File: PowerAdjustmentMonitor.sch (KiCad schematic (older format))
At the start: 19 parts

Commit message: Started Layout Outline.  Completed other schem videos
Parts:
- removed R? (x2): R, ~, symbol R
- removed U? (x2): LM324, symbol LM324
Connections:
- net V+_MON is gone; now on net V+_ADJ: R?.1, U?.3 (OUT)
- net V-_MON is gone; now on net V-_ADJ: R?.2, U?.3 (OUT)
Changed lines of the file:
@@
 $Descr A4 11693 8268
 encoding utf-8
-Sheet 9 9
+Sheet 6 9
 Title ""
-Date "11 feb 2014"
+Date "17 feb 2014"
 Rev ""
 Comp ""
@@
 Connection ~ 3650 1650
 Wire Wire Line
-	3450 1100 4150 1100
-Wire Wire Line
-	4650 1100 5700 1100
+	3450 1100 5700 1100
 Connection ~ 3650 1100
 Text HLabel 5700 1100 2    60   Output ~ 0
@@
 Text HLabel 6750 5450 2    60   Output ~ 0
 V-_ADJ_MON
-Text HLabel 9900 1650 2    60   Output ~ 0
-V+_CURR_MON
-Text HLabel 9800 5750 2    60   Output ~ 0
-V-_CURR_MON
 $Comp
 L R R?
@@
 Wire Wire Line
 	6400 3550 6400 3450
-$Comp
-L R R?
-U 1 1 52F83066
-P 4400 1100
-F 0 "R?" V 4480 1100 40  0000 C CNN
-F 1 "R" V 4407 1101 40  0000 C CNN
-F 2 "~" V 4330 1100 30  0000 C CNN
-F 3 "~" H 4400 1100 30  0000 C CNN
-	1    4400 1100
-	0    -1   -1   0
-$EndComp
-$Comp
-L R R?
-U 1 1 52F830FF
-P 4600 7000
-F 0 "R?" V 4680 7000 40  0000 C CNN
-F 1 "R" V 4607 7001 40  0000 C CNN
-F 2 "~" V 4530 7000 30  0000 C CNN
-F 3 "~" H 4600 7000 30  0000 C CNN
-	1    4600 7000
-	0    -1   -1   0
-$EndComp
-Wire Wire Line
-	3450 7000 4350 7000
-Wire Wire Line
-	4850 7000 5900 7000
-Wire Wire Line
-	3950 1100 3950 1550
-Wire Wire Line
-	3950 1550 8200 1550
+Wire Wire Line
+	3450 7000 5900 7000
 Connection ~ 3950 1100
-Text Label 4150 1550 0    60   ~ 0
-V+_MON
-Wire Wire Line
-	4150 7000 4150 7500
-Wire Wire Line
-	4150 7500 6900 7500
-Connection ~ 4150 7000
-Text Label 4400 7500 0    60   ~ 0
-V-_MON
-$Comp
-L LM324 U?
-U 1 1 52F836D4
-P 8700 1650
-F 0 "U?" H 8750 1850 60  0000 C CNN
-F 1 "LM324" H 8850 1450 50  0000 C CNN
-F 2 "" H 8700 1650 60  0000 C CNN
-F 3 "" H 8700 1650 60  0000 C CNN
-	1    8700 1650
-	1    0    0    -1
-$EndComp
-$Comp
-L +12V #PWR?
-U 1 1 52F836ED
-P 8600 1150
-F 0 "#PWR?" H 8600 1100 20  0001 C CNN
-F 1 "+12V" H 8600 1250 30  0000 C CNN
-F 2 "" H 8600 1150 60  0000 C CNN
-F 3 "" H 8600 1150 60  0000 C CNN
-	1    8600 1150
-	1    0    0    -1
-$EndComp
-$Comp
-L -12V #PWR?
-U 1 1 52F836F3
-P 8950 2100
-F 0 "#PWR?" H 8950 2230 20  0001 C CNN
-F 1 "-12V" H 8950 2200 30  0000 C CNN
-F 2 "" H 8950 2100 60  0000 C CNN
-F 3 "" H 8950 2100 60  0000 C CNN
-	1    8950 2100
-	1    0    0    -1
-$EndComp
-Wire Wire Line
-	8200 1750 8050 1750
-Wire Wire Line
-	8050 1750 8050 2250
-Wire Wire Line
-	8050 2250 9350 2250
-Wire Wire Line
-	9350 2250 9350 1650
-Wire Wire Line
-	9200 1650 9900 1650
-Wire Wire Line
-	8600 2050 8600 2150
-Wire Wire Line
-	8600 2150 8950 2150
-Wire Wire Line
-	8950 2150 8950 2100
-Wire Wire Line
-	8600 1250 8600 1150
-Connection ~ 9350 1650
-$Comp
-L LM324 U?
-U 1 1 52F8384E
-P 8600 5750
-F 0 "U?" H 8650 5950 60  0000 C CNN
-F 1 "LM324" H 8750 5550 50  0000 C CNN
-F 2 "" H 8600 5750 60  0000 C CNN
-F 3 "" H 8600 5750 60  0000 C CNN
-	1    8600 5750
-	1    0    0    -1
-$EndComp
-$Comp
-L +12V #PWR?
-U 1 1 52F83854
-P 8500 5250
-F 0 "#PWR?" H 8500 5200 20  0001 C CNN
-F 1 "+12V" H 8500 5350 30  0000 C CNN
-F 2 "" H 8500 5250 60  0000 C CNN
-F 3 "" H 8500 5250 60  0000 C CNN
-	1    8500 5250
-	1    0    0    -1
-$EndComp
-$Comp
-L -12V #PWR?
-U 1 1 52F8385A
-P 8850 6200
-F 0 "#PWR?" H 8850 6330 20  0001 C CNN
-F 1 "-12V" H 8850 6300 30  0000 C CNN
-F 2 "" H 8850 6200 60  0000 C CNN
-F 3 "" H 8850 6200 60  0000 C CNN
-	1    8850 6200
-	1    0    0    -1
-$EndComp
-Wire Wire Line
-	8100 5850 7950 5850
-Wire Wire Line
-	7950 5850 7950 6350
-Wire Wire Line
-	7950 6350 9250 6350
-Wire Wire Line
-	9250 6350 9250 5750
-Wire Wire Line
-	9100 5750 9800 5750
-Wire Wire Line
-	8500 6150 8500 6250
-Wire Wire Line
-	8500 6250 8850 6250
-Wire Wire Line
-	8850 6250 8850 6200
-Wire Wire Line
-	8500 5350 8500 5250
-Connection ~ 9250 5750
-Wire Wire Line
-	6900 7500 6900 5650
-Wire Wire Line
-	6900 5650 8100 5650
 $Comp
 L RVAR R?

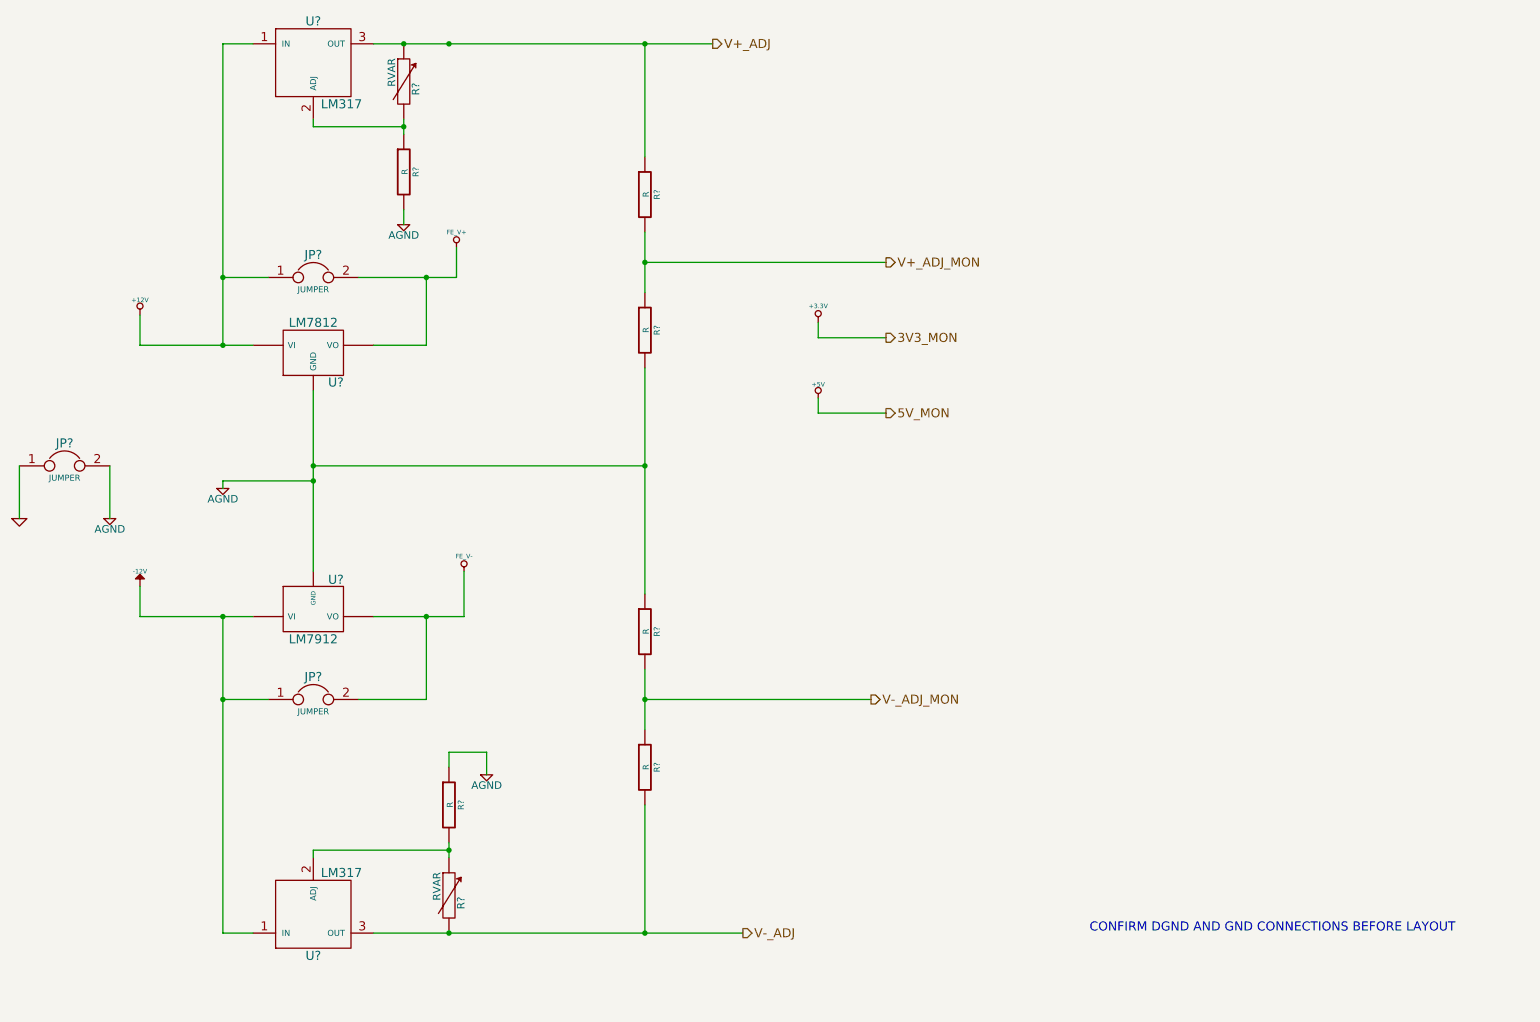
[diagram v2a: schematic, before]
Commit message: started associating relay parts
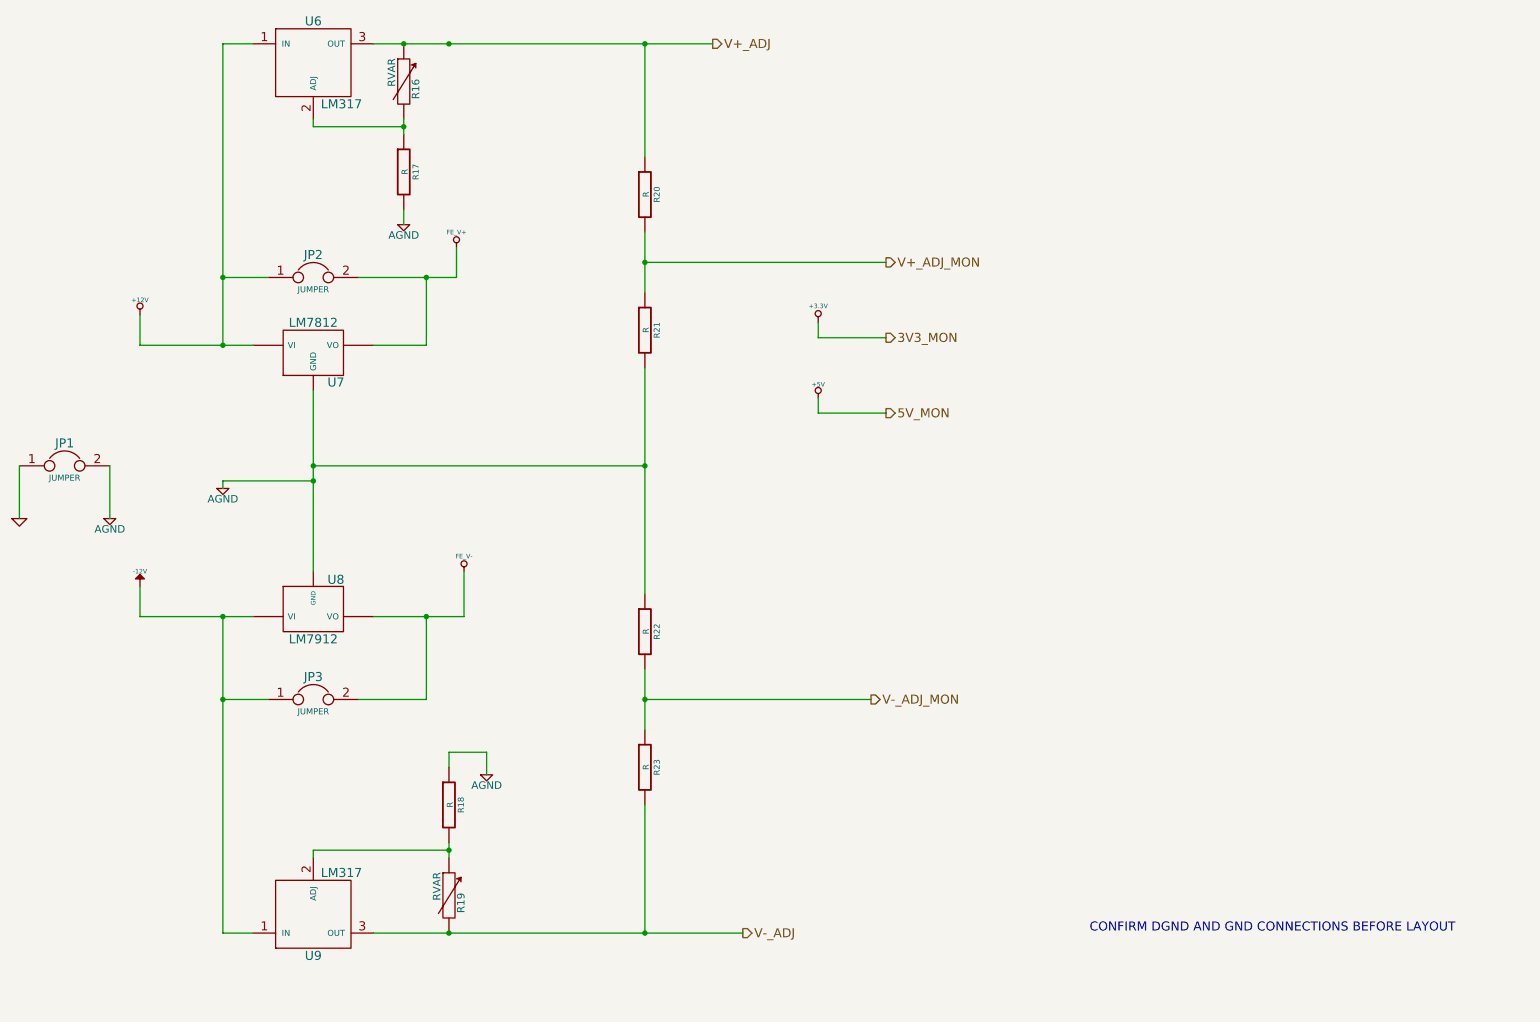
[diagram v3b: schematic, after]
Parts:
- gave numbers to parts that had none: 15
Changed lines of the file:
@@
 Sheet 6 9
 Title ""
-Date "17 feb 2014"
+Date "20 feb 2014"
 Rev ""
 Comp ""
@@
 $EndDescr
 $Comp
-L GND #PWR?
+L GND #PWR030
 U 1 1 52F6B17F
 P 1100 4250
-F 0 "#PWR?" H 1100 4250 30  0001 C CNN
+F 0 "#PWR030" H 1100 4250 30  0001 C CNN
 F 1 "GND" H 1100 4180 30  0001 C CNN
 F 2 "" H 1100 4250 60  0000 C CNN
@@
 CONFIRM DGND AND GND CONNECTIONS BEFORE LAYOUT
 $Comp
-L +5V #PWR?
+L +5V #PWR031
 U 1 1 52F6B186
 P 6400 3450
-F 0 "#PWR?" H 6400 3540 20  0001 C CNN
+F 0 "#PWR031" H 6400 3540 20  0001 C CNN
 F 1 "+5V" H 6400 3540 30  0000 C CNN
 F 2 "" H 6400 3450 60  0000 C CNN
@@
 $EndComp
 $Comp
-L +3.3V #PWR?
+L +3.3V #PWR032
 U 1 1 52F6B18C
 P 6400 2950
-F 0 "#PWR?" H 6400 2910 30  0001 C CNN
+F 0 "#PWR032" H 6400 2910 30  0001 C CNN
 F 1 "+3.3V" H 6400 3060 30  0000 C CNN
 F 2 "" H 6400 2950 60  0000 C CNN
@@
 $EndComp
 $Comp
-L +12V #PWR?
+L +12V #PWR033
 U 1 1 52F6B215
 P 1900 2900
-F 0 "#PWR?" H 1900 2850 20  0001 C CNN
+F 0 "#PWR033" H 1900 2850 20  0001 C CNN
 F 1 "+12V" H 1900 3000 30  0000 C CNN
 F 2 "" H 1900 2900 60  0000 C CNN
@@
 $EndComp
 $Comp
-L -12V #PWR?
+L -12V #PWR034
 U 1 1 52F6B21C
 P 1900 4700
-F 0 "#PWR?" H 1900 4830 20  0001 C CNN
+F 0 "#PWR034" H 1900 4830 20  0001 C CNN
 F 1 "-12V" H 1900 4800 30  0000 C CNN
 F 2 "" H 1900 4700 60  0000 C CNN
@@
 	1900 3100 1900 2900
 $Comp
-L LM317 U?
+L LM317 U6
 U 1 1 52F81AFB
 P 3050 1250
-F 0 "U?" H 3050 1550 60  0000 C CNN
+F 0 "U6" H 3050 1550 60  0000 C CNN
 F 1 "LM317" H 3100 1000 60  0000 L CNN
 F 2 "~" H 3050 1250 60  0000 C CNN
@@
 $EndComp
 $Comp
-L LM317 U?
+L LM317 U9
 U 1 1 52F81B73
 P 3050 6850
-F 0 "U?" H 3050 7150 60  0000 C CNN
+F 0 "U9" H 3050 7150 60  0000 C CNN
 F 1 "LM317" H 3100 6600 60  0000 L CNN
 F 2 "~" H 3050 6850 60  0000 C CNN
@@
 	3050 3400 3050 4600
 $Comp
-L JUMPER JP?
+L JUMPER JP3
 U 1 1 52F81B9A
 P 3050 5450
-F 0 "JP?" H 3050 5600 60  0000 C CNN
+F 0 "JP3" H 3050 5600 60  0000 C CNN
 F 1 "JUMPER" H 3050 5370 40  0000 C CNN
 F 2 "~" H 3050 5450 60  0000 C CNN
@@
 $EndComp
 $Comp
-L JUMPER JP?
+L JUMPER JP2
 U 1 1 52F81BA7
 P 3050 2650
-F 0 "JP?" H 3050 2800 60  0000 C CNN
+F 0 "JP2" H 3050 2800 60  0000 C CNN
 F 1 "JUMPER" H 3050 2570 40  0000 C CNN
 F 2 "~" H 3050 2650 60  0000 C CNN
@@
 	1900 3100 2650 3100
 $Comp
-L AGND #PWR?
+L AGND #PWR035
 U 1 1 52F81DE2
 P 1700 4250
-F 0 "#PWR?" H 1700 4250 40  0001 C CNN
+F 0 "#PWR035" H 1700 4250 40  0001 C CNN
 F 1 "AGND" H 1700 4180 50  0000 C CNN
 F 2 "" H 1700 4250 60  0000 C CNN
@@
 $EndComp
 $Comp
-L JUMPER JP?
+L JUMPER JP1
 U 1 1 52F81DF9
 P 1400 3900
-F 0 "JP?" H 1400 4050 60  0000 C CNN
+F 0 "JP1" H 1400 4050 60  0000 C CNN
 F 1 "JUMPER" H 1400 3820 40  0000 C CNN
 F 2 "~" H 1400 3900 60  0000 C CNN
@@
 	1700 4250 1700 3900
 $Comp
-L AGND #PWR?
+L AGND #PWR036
 U 1 1 52F81E20
 P 2450 4050
-F 0 "#PWR?" H 2450 4050 40  0001 C CNN
+F 0 "#PWR036" H 2450 4050 40  0001 C CNN
 F 1 "AGND" H 2450 3980 50  0000 C CNN
 F 2 "" H 2450 4050 60  0000 C CNN
@@
 	3350 5450 3800 5450
 $Comp
-L FE_V+ #PWR?
+L FE_V+ #PWR037
 U 1 1 52F82106
 P 4000 2450
-F 0 "#PWR?" H 4000 2550 30  0001 C CNN
+F 0 "#PWR037" H 4000 2550 30  0001 C CNN
 F 1 "FE_V+" H 4000 2550 30  0000 C CNN
 F 2 "" H 4000 2450 60  0000 C CNN
@@
 Connection ~ 3800 2650
 $Comp
-L FE_V- #PWR?
+L FE_V- #PWR038
 U 1 1 52F8214F
 P 4050 4600
-F 0 "#PWR?" H 4050 4700 30  0001 C CNN
+F 0 "#PWR038" H 4050 4700 30  0001 C CNN
 F 1 "FE_V-" H 4050 4700 30  0000 C CNN
 F 2 "" H 4050 4600 60  0000 C CNN
@@
 Connection ~ 3800 4900
 $Comp
-L LM7812 U?
+L LM7812 U7
 U 1 1 52F82388
 P 3050 3150
-F 0 "U?" H 3200 2954 60  0000 C CNN
+F 0 "U7" H 3200 2954 60  0000 C CNN
 F 1 "LM7812" H 3050 3350 60  0000 C CNN
 F 2 "~" H 3050 3150 60  0000 C CNN
@@
 $EndComp
 $Comp
-L LM7912 U?
+L LM7912 U8
 U 1 1 52F823B2
 P 3050 4850
-F 0 "U?" H 3200 4655 60  0000 C CNN
+F 0 "U8" H 3200 4655 60  0000 C CNN
 F 1 "LM7912" H 3050 5050 60  0000 C CNN
 F 2 "~" H 3050 4850 60  0000 C CNN
@@
 Connection ~ 2450 5450
 $Comp
-L R R?
+L R R18
 U 1 1 52F82656
 P 3950 6150
-F 0 "R?" V 4030 6150 40  0000 C CNN
+F 0 "R18" V 4030 6150 40  0000 C CNN
 F 1 "R" V 3957 6151 40  0000 C CNN
 F 2 "~" V 3880 6150 30  0000 C CNN
@@
 Connection ~ 3950 6450
 $Comp
-L AGND #PWR?
+L AGND #PWR039
 U 1 1 52F826DB
 P 4200 5950
-F 0 "#PWR?" H 4200 5950 40  0001 C CNN
+F 0 "#PWR039" H 4200 5950 40  0001 C CNN
 F 1 "AGND" H 4200 5880 50  0000 C CNN
 F 2 "" H 4200 5950 60  0000 C CNN
@@
 Connection ~ 3950 7000
 $Comp
-L R R?
+L R R17
 U 1 1 52F82737
 P 3650 1950
-F 0 "R?" V 3730 1950 40  0000 C CNN
+F 0 "R17" V 3730 1950 40  0000 C CNN
 F 1 "R" V 3657 1951 40  0000 C CNN
 F 2 "~" V 3580 1950 30  0000 C CNN
@@
 	3650 1600 3650 1700
 $Comp
-L AGND #PWR?
+L AGND #PWR040
 U 1 1 52F82746
 P 3650 2300
-F 0 "#PWR?" H 3650 2300 40  0001 C CNN
+F 0 "#PWR040" H 3650 2300 40  0001 C CNN
 F 1 "AGND" H 3650 2230 50  0000 C CNN
 F 2 "" H 3650 2300 60  0000 C CNN
@@
 V-_ADJ_MON
 $Comp
-L R R?
+L R R20
 U 1 1 52F82AEB
 P 5250 2100
-F 0 "R?" V 5330 2100 40  0000 C CNN
+F 0 "R20" V 5330 2100 40  0000 C CNN
 F 1 "R" V 5257 2101 40  0000 C CNN
 F 2 "~" V 5180 2100 30  0000 C CNN
@@
 $EndComp
 $Comp
-L R R?
+L R R21
 U 1 1 52F82B05
 P 5250 3000
-F 0 "R?" V 5330 3000 40  0000 C CNN
+F 0 "R21" V 5330 3000 40  0000 C CNN
 F 1 "R" V 5257 3001 40  0000 C CNN
 F 2 "~" V 5180 3000 30  0000 C CNN
@@
 Connection ~ 3050 3900
 $Comp
-L R R?
+L R R22
 U 1 1 52F82BE2
 P 5250 5000
-F 0 "R?" V 5330 5000 40  0000 C CNN
+F 0 "R22" V 5330 5000 40  0000 C CNN
 F 1 "R" V 5257 5001 40  0000 C CNN
 F 2 "~" V 5180 5000 30  0000 C CNN
@@
 $EndComp
 $Comp
-L R R?
+L R R23
 U 1 1 52F82BF2
 P 5250 5900
-F 0 "R?" V 5330 5900 40  0000 C CNN
+F 0 "R23" V 5330 5900 40  0000 C CNN
 F 1 "R" V 5257 5901 40  0000 C CNN
 F 2 "~" V 5180 5900 30  0000 C CNN
@@
 Connection ~ 3950 1100
 $Comp
-L RVAR R?
+L RVAR R16
 U 1 1 52F83BA4
 P 3650 1350
-F 0 "R?" V 3730 1300 50  0000 C CNN
+F 0 "R16" V 3730 1300 50  0000 C CNN
 F 1 "RVAR" V 3570 1410 50  0000 C CNN
 F 2 "~" H 3650 1350 60  0000 C CNN
@@
 $EndComp
 $Comp
-L RVAR R?
+L RVAR R19
 U 1 1 52F83BBB
 P 3950 6750
-F 0 "R?" V 4030 6700 50  0000 C CNN
+F 0 "R19" V 4030 6700 50  0000 C CNN
 F 1 "RVAR" V 3870 6810 50  0000 C CNN
 F 2 "~" H 3950 6750 60  0000 C CNN
